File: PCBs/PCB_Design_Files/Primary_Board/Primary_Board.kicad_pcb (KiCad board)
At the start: 4 copper layers, 40.3 x 57.1 mm, 119 parts, among them J1 Conn_FFC_8pin, J2 Conn_01x08_Pin, U1 OPA381, U10 TMUX1133PWR, U11 MCP6561T-E/OT, U12 TMUX1133PWR, U13 LF398N/NOPB, U14 AD5621AKSZ, U15 TMUX1133PWR, U2 TLV9002, U3 REF3333AIDBZR, U4 TLV9002, U5 MOUDLE-SEEEDUINO-XIAO-ESP32C3, U6 DM-OLED096-636, U7 TMUX1104DGSR, U8 TMUX1133PWR, U9 TMUX1133PWR

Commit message: saved
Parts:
- added ESP_3V3: 3V3 Bypass, Jumper:SolderJumper-2_P1.3mm_Open_Pad1.0x1.5mm, F.Cu at (111.1, 132.2)
- added R22: 4.7k, Resistor_SMD:R_0402_1005Metric, F.Cu at (106.2, 131.4)
- added R23: 4.7k, Resistor_SMD:R_0402_1005Metric, F.Cu at (106.2, 133.4)
- moved U13 92.0 mm to (162.7, 96.9), turned to 180 degrees
- moved U3 77.6 mm to (154.9, 76.8), turned to 0 degrees
- moved C10 77.4 mm to (152.3, 76.8), turned to -90 degrees
- moved R14 75.4 mm to (157.6, 78.7), turned to -90 degrees
- moved R16 75.2 mm to (156.6, 78.7), turned to -90 degrees
- moved C11 74.5 mm to (155.0, 79.1), turned to 180 degrees
- moved R15 74.3 mm to (161.7, 80.3), turned to -90 degrees
- moved R13 74.0 mm to (160.6, 80.3), turned to -90 degrees
- moved C30 73.2 mm to (158.6, 80.5), turned to 0 degrees
- moved U11 72.9 mm to (130.7, 88.3), turned to 180 degrees
- moved C32 72.6 mm to (155.6, 80.5), turned to 180 degrees
- moved C31 72.2 mm to (162.7, 82.1), turned to 0 degrees
- moved C29 71.3 mm to (159.6, 82.1), turned to 180 degrees
- moved R12 70.8 mm to (163.6, 83.4), turned to 0 degrees
- moved C12 70.2 mm to (156.6, 82.3), turned to 90 degrees
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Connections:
- U5 pad 10: unconnected-(U5-PA5_A9_D9_MISO-Pad10) -> /ADC/A0
- U5 pad 11: unconnected-(U5-PA6_A10_D10_MOSI-Pad11) -> /ADC/MOSI
- U5 pad 12: unconnected-(U5-3V3-Pad12) -> Net-(ESP_3V3-A)
- U5 pad 13: unconnected-(U5-GND-Pad13) -> GND
- U5 pad 14: unconnected-(U5-5V-Pad14) -> +5V
- U5 pad 2: unconnected-(U5-PA4_A1_D1-Pad2) -> /ADC/CS
- U5 pad 3: unconnected-(U5-PA10_A2_D2-Pad3) -> /ADC/LATCH
- U5 pad 5: unconnected-(U5-PA8_A4_D4_SDA-Pad5) -> Net-(U5-PA8_A4_D4_SDA)
- U5 pad 6: unconnected-(U5-PA9_A5_D5_SCL-Pad6) -> Net-(U5-PA9_A5_D5_SCL)
- U5 pad 8: unconnected-(U5-PB09_A7_D7_RX-Pad8) -> /ADC/A1
- U5 pad 9: unconnected-(U5-PA7_A8_D8_SCK-Pad9) -> /ADC/sCLK
- U6 pad 1: unconnected-(U6-GND-Pad1) -> GND
- U6 pad 2: unconnected-(U6-VCC_IN-Pad2) -> +5V
- U6 pad 3: unconnected-(U6-SCL-Pad3) -> Net-(U5-PA9_A5_D5_SCL)
- U6 pad 4: unconnected-(U6-SDA-Pad4) -> Net-(U5-PA8_A4_D4_SDA)
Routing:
- net /ADC/BIT_13_SEL: track 0.00 -> 2.95 mm, vias 0 -> 2
- net GND: track 22.9 -> 20.3 mm, vias 15 -> 12
- net +3V3: track 6.70 -> 5.20 mm, vias 5 -> 3
- net /ADC/BIT_12_SEL: track 0.00 -> 1.16 mm, vias 0 -> 1
- net Net-(C5-Pad2): vias 2 -> 3
- net /ADC/BIT_1_SEL: vias 0 -> 1

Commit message: 3rd order filter
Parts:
- added C68: 220n, Project Footprints:0603_capacitor, B.Cu at (144.1, 102.8)
- added R17: 100k, Project Footprints:0603_resistor, B.Cu at (141.8, 102.7)
- moved R4 0.78 mm to (139.2, 102.7)
- moved R5 0.33 mm to (136.3, 102.7)
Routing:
- net Net-(C68-Pad1): track 0.00 -> 6.12 mm
- net /AFE/+1.65V: track 12.0 -> 15.0 mm
- net /ADC/BIT_13_SEL: track 2.95 -> 0.00 mm, vias 2 -> 1
- net Net-(C5-Pad2): track 14.6 -> 13.1 mm
- net GND: track 20.3 -> 18.8 mm, vias 12 -> 8
- net (no net): track 1.30 -> 0.00 mm
- net /ADC/BIT_12_SEL: track 1.16 -> 0.00 mm
- net /AFE/TIA_OUT: track 17.2 -> 16.5 mm
- net Net-(U2-IN2-): vias 2 -> 1

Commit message: Layed out all components, need to route
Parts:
- added C70: 100nF, Capacitor_SMD:C_0402_1005Metric, F.Cu at (163.6, 120.0)
- added C71: 100pF, Capacitor_SMD:C_0402_1005Metric, B.Cu at (149.6, 114.9)
- added C72: 100nF, Capacitor_SMD:C_0402_1005Metric, F.Cu at (158.0, 109.2)
- added SH1: ADG701BRJZ-REEL7, Package_TO_SOT_SMD:SOT-23-5_HandSoldering, F.Cu at (161.3, 118.2)
- C48, C54, C64, ESP_3V3, R22, R23, SR1, SR2, U14: moved to B.Cu
- R18: value 1k -> 100; moved to B.Cu
- R19: value 1k -> 100
- U13: value LF398N/NOPB -> OPA320SAIDBVR; footprint Package_DIP:DIP-8_W7.62mm -> Package_TO_SOT_SMD:SOT-23-6_Handsoldering
- moved C20 136.9 mm to (160.3, 81.3), turned to 90 degrees
- moved C19 136.9 mm to (158.7, 81.3), turned to 90 degrees
- moved C4 135.9 mm to (163.4, 86.9), turned to -90 degrees
- moved C18 135.6 mm to (157.2, 81.3), turned to 90 degrees
- moved C52 134.6 mm to (162.5, 83.6)
- moved C17 134.5 mm to (155.7, 81.3), turned to 90 degrees
- moved C56 133.9 mm to (162.5, 82.1)
- moved C16 133.4 mm to (154.2, 81.3), turned to 90 degrees
- moved C49 133.1 mm to (160.3, 84.3), turned to -90 degrees
- moved C15 132.3 mm to (152.7, 81.3), turned to 90 degrees
- moved C46 132.2 mm to (158.8, 84.3), turned to -90 degrees
- moved C42 131.7 mm to (157.2, 84.3), turned to -90 degrees
- moved C14 131.3 mm to (151.1, 81.3), turned to 90 degrees
- moved C41 130.6 mm to (155.7, 84.3), turned to -90 degrees
- moved C13 130.4 mm to (149.6, 81.3), turned to 90 degrees
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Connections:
- C65 pad 1: Net-(C65-Pad1) -> /ADC/HOLD
- R18 pad 1: /ADC/S/H_IN -> Net-(U14-VOUT)
- R18 pad 2: Net-(S/H1-B) -> /ADC/DAC_OUT
- R19 pad 1: GND -> /ADC/S/H_OUT
- R19 pad 2: /ADC/S/H_IN -> Net-(U13A--)
- U13 pad 1: +5V -> Net-(U13A--)
- U13 pad 2: unconnected-(U13-Pad2) -> GND
- U13 pad 3: /ADC/S/H_IN -> /ADC/HOLD
- U13 pad 4: GND -> Net-(U13A--)
- U13 pad 5: /ADC/S/H_OUT -> (no net)
- U13 pad 6: Net-(C65-Pad1) -> +3V3A
- U14 pad 6: /ADC/DAC_OUT -> Net-(U14-VOUT)
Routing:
- net /ADC/VSMP: track 0.00 -> 82.3 mm
- net /ADC/LSB_TOP: track 0.00 -> 30.5 mm
- net /ADC/MSB_TOP: track 0.00 -> 30.4 mm, vias 0 -> 1
- net /V_bandgap: track 51.9 -> 27.6 mm, vias 1 -> 0
- net /V_ptat: track 0.00 -> 18.4 mm, vias 0 -> 1
- net GND: track 18.8 -> 35.9 mm, vias 8 -> 9
- net /ADC/BIT_13_BOT: track 0.00 -> 11.8 mm, vias 0 -> 1
- net /ADC/BIT_6_BOT: track 0.00 -> 11.8 mm, vias 0 -> 1
- net +5V: track 0.07 -> 8.41 mm
- net Net-(C5-Pad2): track 13.1 -> 5.24 mm, vias 3 -> 0
- net Net-(U7-S4): track 0.00 -> 7.35 mm
- net Net-(U7-S2): track 0.00 -> 7.21 mm
- net /ADC/BIT_12_BOT: track 0.00 -> 5.70 mm, vias 0 -> 1
- net Net-(U7-S1): track 0.00 -> 5.56 mm
- net Net-(U2-IN2-): track 16.7 -> 11.5 mm, vias 1 -> 0
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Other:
- board text added: "LSB"
- board text added: "MSB"

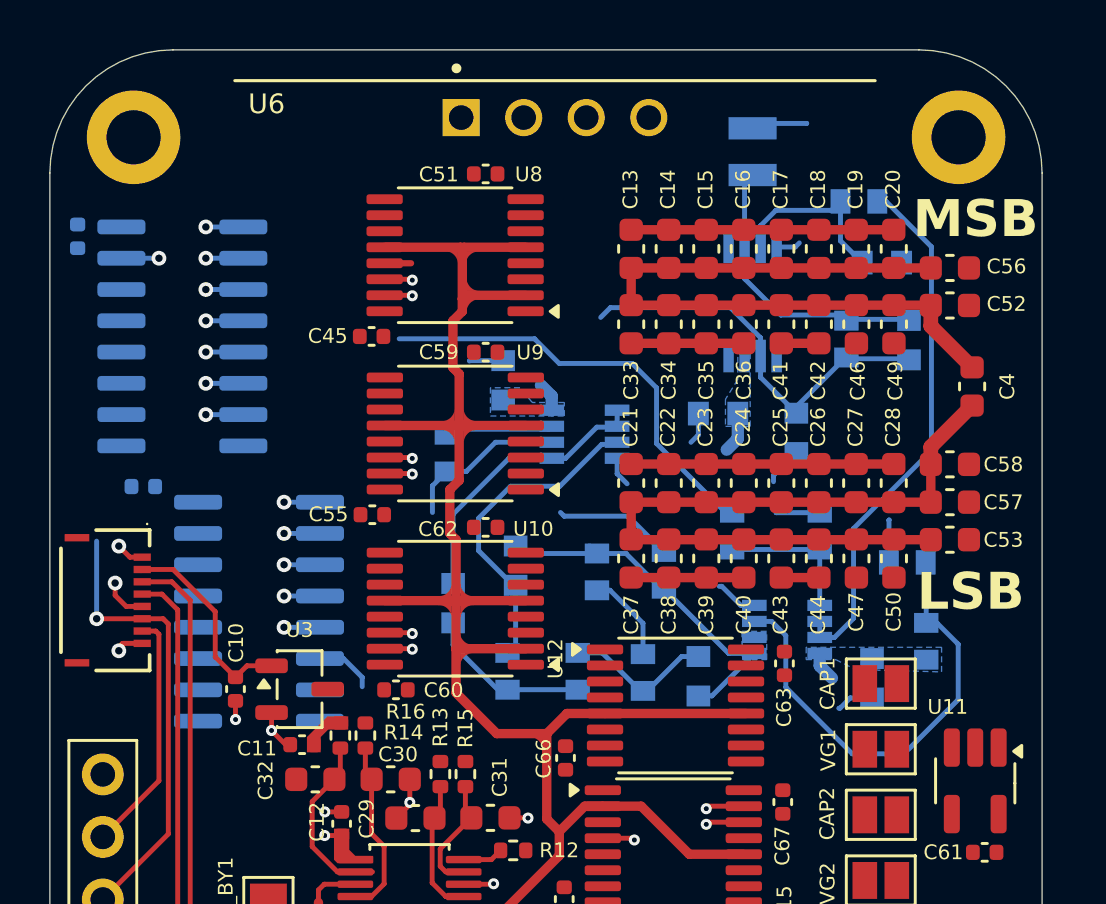
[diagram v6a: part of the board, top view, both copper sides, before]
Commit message: fixed AFE layout
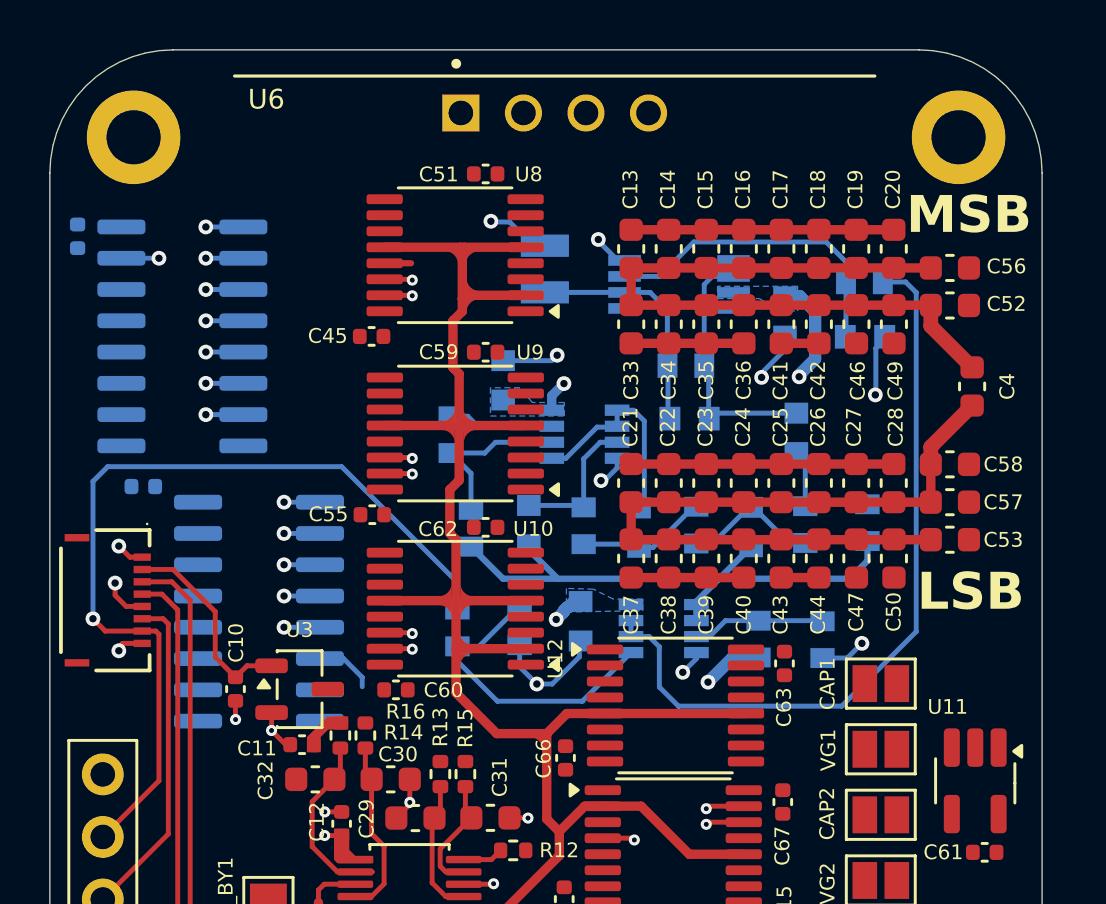
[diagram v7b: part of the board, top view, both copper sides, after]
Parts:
- moved R11 12.8 mm to (145.1, 96.6), turned to -90 degrees
- moved C9 12.1 mm to (147.6, 96.4)
- moved R10 11.8 mm to (142.6, 96.7)
- moved R3 11.2 mm to (159.2, 92.4), turned to -90 degrees
- moved LED1 9.69 mm to (146.1, 82.1)
- moved C2 9.46 mm to (152.0, 88.2), turned to 0 degrees
- moved R17 8.92 mm to (156.7, 92.5)
- moved C6 8.15 mm to (149.9, 92.6)
- moved R6 8.02 mm to (143.1, 92.6)
- moved R4 7.64 mm to (152.2, 92.5), turned to 90 degrees
- moved R8 6.81 mm to (154.8, 97.1)
- moved R5 6.67 mm to (147.7, 92.5)
- moved R2 6.61 mm to (151.8, 86.0), turned to 0 degrees
- moved C68 6.43 mm to (154.5, 92.6)
- moved U4 5.01 mm to (150.9, 96.7), turned to 180 degrees
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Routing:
- net Net-(U4-IN1+): track 19.0 -> 5.40 mm
- net /AFE/Vref: track 21.7 -> 30.9 mm
- net /AFE/+1.65V: track 15.0 -> 23.8 mm
- net /V_bandgap: track 27.6 -> 35.7 mm, vias 0 -> 1
- net Net-(U2-IN1+): track 13.1 -> 5.99 mm
- net Net-(U4-IN2+): track 5.83 -> 12.3 mm
- net /AFE/TIA_OUT: track 16.5 -> 10.4 mm
- net GND: track 35.9 -> 41.5 mm, vias 9 -> 18
- net Net-(U1-IN+): track 7.37 -> 13.0 mm
- net +3V3: track 5.88 -> 11.3 mm, vias 2 -> 6
- net /V_ptat: track 18.4 -> 13.4 mm, vias 1 -> 0
- net Net-(U2-IN2-): track 11.5 -> 6.93 mm
- net Net-(U2-IN1-): track 11.6 -> 8.84 mm
- net /AFE/PD_Out: track 11.9 -> 9.71 mm
- net Net-(C6-Pad1): track 7.05 -> 5.38 mm
- removed copper zone on B.Cu, net /AFE/+1.65V
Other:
- board text added: "Gnd Vbandgap Vptat Gnd PwmIR PwmRed 5V 3v3"
- board text removed: "Gnd Vptat Vbandgap Gnd PwmIR PwmRed Gnd 3v3"

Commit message: Routing Cont
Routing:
- net GND: track 41.5 -> 95.4 mm, vias 18 -> 36
- net /ADC/LATCH: track 0.00 -> 34.1 mm, vias 0 -> 2
- net /ADC/BIT_7_BOT: track 1.13 -> 26.3 mm
- net /ADC/sCLK: track 0.00 -> 23.6 mm, vias 0 -> 2
- net /ADC/MOSI: track 0.00 -> 22.7 mm
- net /ADC/BIT_3_SEL: track 1.46 -> 22.2 mm
- net /ADC/BIT_1_SEL: track 1.46 -> 21.9 mm
- net /ADC/BIT_0_SEL: track 1.46 -> 21.6 mm
- net /ADC/BIT_2_SEL: track 1.46 -> 21.5 mm
- net /ADC/BIT_10_BOT: track 1.13 -> 21.1 mm
- net +3V3: track 11.3 -> 31.0 mm, vias 6 -> 15
- net /ADC/BIT_9_BOT: track 1.12 -> 20.5 mm
- net /ADC/TOP_RESET: track 2.41 -> 21.4 mm, vias 0 -> 1
- net /ADC/BIT_8_SEL: track 1.52 -> 16.3 mm
- net /ADC/BIT_6_BOT: track 11.8 -> 24.5 mm
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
